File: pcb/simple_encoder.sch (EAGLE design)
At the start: 11 parts, among them X1 PEC11R

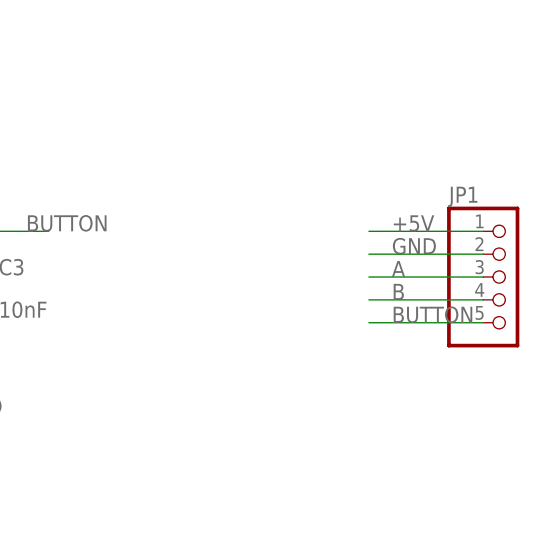
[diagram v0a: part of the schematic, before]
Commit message: updated simple controller, simple encoder (3D Packages)
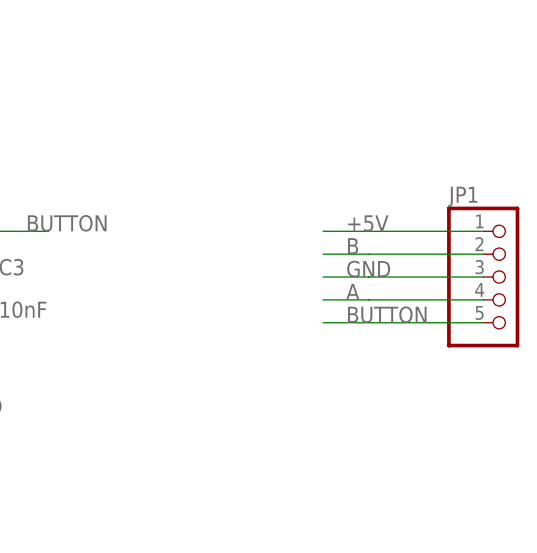
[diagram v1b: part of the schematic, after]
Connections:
- net A: now also JP1.4; no longer JP1.3
- net B: now also JP1.2; no longer JP1.4
- net GND: now also JP1.3; no longer JP1.2
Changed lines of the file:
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@@
 <part name="C1" library="rcl" library_urn="urn:adsk.eagle:library:334" deviceset="C-EU" device="C0805" package3d_urn="urn:adsk.eagle:package:23617/2" value="10nF"/>
 <part name="R2" library="rcl" library_urn="urn:adsk.eagle:library:334" deviceset="R-EU_" device="R0805" package3d_urn="urn:adsk.eagle:package:23553/2" value="10k"/>
-<part name="X1" library="solderpi" library_urn="urn:adsk.eagle:library:1437534" deviceset="PEC11R" device=""/>
+<part name="X1" library="solderpi" library_urn="urn:adsk.eagle:library:1437534" deviceset="PEC11R" device="" package3d_urn="urn:adsk.eagle:package:3057193/4"/>
 <part name="P+1" library="supply1" library_urn="urn:adsk.eagle:library:371" deviceset="+5V" device=""/>
 <part name="GND1" library="supply1" library_urn="urn:adsk.eagle:library:371" deviceset="GND" device=""/>
@@
 </segment>
 <segment>
-<pinref part="JP1" gate="A" pin="2"/>
-<wire x1="190.5" y1="121.92" x2="177.8" y2="121.92" width="0.1524" layer="91"/>
-<label x="180.34" y="121.92" size="1.778" layer="95"/>
+<pinref part="JP1" gate="A" pin="3"/>
+<wire x1="190.5" y1="119.38" x2="177.8" y2="119.38" width="0.1524" layer="91"/>
+<wire x1="177.8" y1="119.38" x2="172.72" y2="119.38" width="0.1524" layer="91"/>
+<label x="175.26" y="119.38" size="1.778" layer="95"/>
 </segment>
 </net>
@@
 </segment>
 <segment>
-<pinref part="JP1" gate="A" pin="4"/>
-<wire x1="190.5" y1="116.84" x2="177.8" y2="116.84" width="0.1524" layer="91"/>
-<label x="180.34" y="116.84" size="1.778" layer="95"/>
+<pinref part="JP1" gate="A" pin="2"/>
+<wire x1="190.5" y1="121.92" x2="177.8" y2="121.92" width="0.1524" layer="91"/>
+<wire x1="177.8" y1="121.92" x2="172.72" y2="121.92" width="0.1524" layer="91"/>
+<label x="175.26" y="121.92" size="1.778" layer="95"/>
 </segment>
 </net>
@@
 </segment>
 <segment>
-<pinref part="JP1" gate="A" pin="3"/>
-<wire x1="190.5" y1="119.38" x2="177.8" y2="119.38" width="0.1524" layer="91"/>
-<label x="180.34" y="119.38" size="1.778" layer="95"/>
+<pinref part="JP1" gate="A" pin="4"/>
+<wire x1="190.5" y1="116.84" x2="177.8" y2="116.84" width="0.1524" layer="91"/>
+<wire x1="177.8" y1="116.84" x2="172.72" y2="116.84" width="0.1524" layer="91"/>
+<label x="175.26" y="116.84" size="1.778" layer="95"/>
 </segment>
 </net>
@@
 <pinref part="JP1" gate="A" pin="1"/>
 <wire x1="190.5" y1="124.46" x2="177.8" y2="124.46" width="0.1524" layer="91"/>
-<label x="180.34" y="124.46" size="1.778" layer="95"/>
+<label x="175.26" y="124.46" size="1.778" layer="95"/>
+<wire x1="177.8" y1="124.46" x2="172.72" y2="124.46" width="0.1524" layer="91"/>
 </segment>
 </net>
@@
 <pinref part="JP1" gate="A" pin="5"/>
 <wire x1="190.5" y1="114.3" x2="177.8" y2="114.3" width="0.1524" layer="91"/>
-<label x="180.34" y="114.3" size="1.778" layer="95"/>
-</segment>
-</net>
+<label x="175.26" y="114.3" size="1.778" layer="95"/>
+<wire x1="177.8" y1="114.3" x2="172.72" y2="114.3" width="0.1524" layer="91"/>
+</segment>
+</net>
